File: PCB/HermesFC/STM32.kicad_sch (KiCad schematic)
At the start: 46 parts, among them J1 Conn_01x04, J2 Conn_01x04, J3 Conn_01x04, J4 Conn_01x04, J5 Conn_01x06, J6 USB_B_Micro, SW1 SW_Push, SW2 SW_SPDT, U1 STM32F405RGTx, U2 AMS1117-3.3, U3 USBLC6-2SC6, Y1 16Mhz

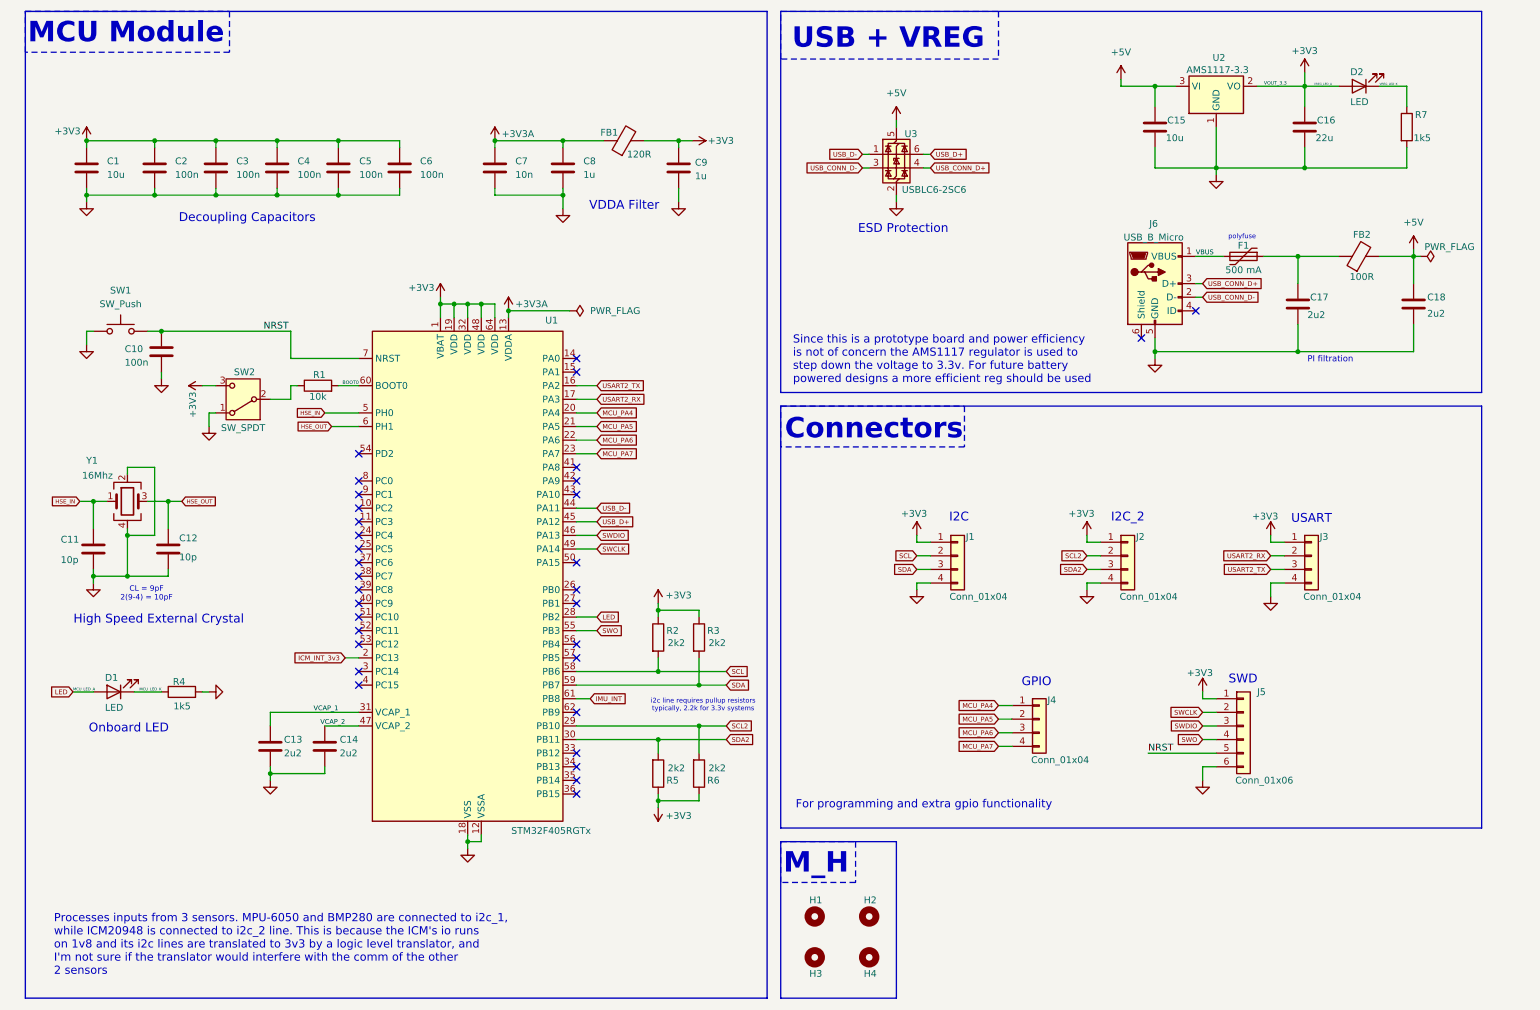
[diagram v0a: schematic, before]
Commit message: v0.2 updated schematic + PCB
added battery power source to PCB
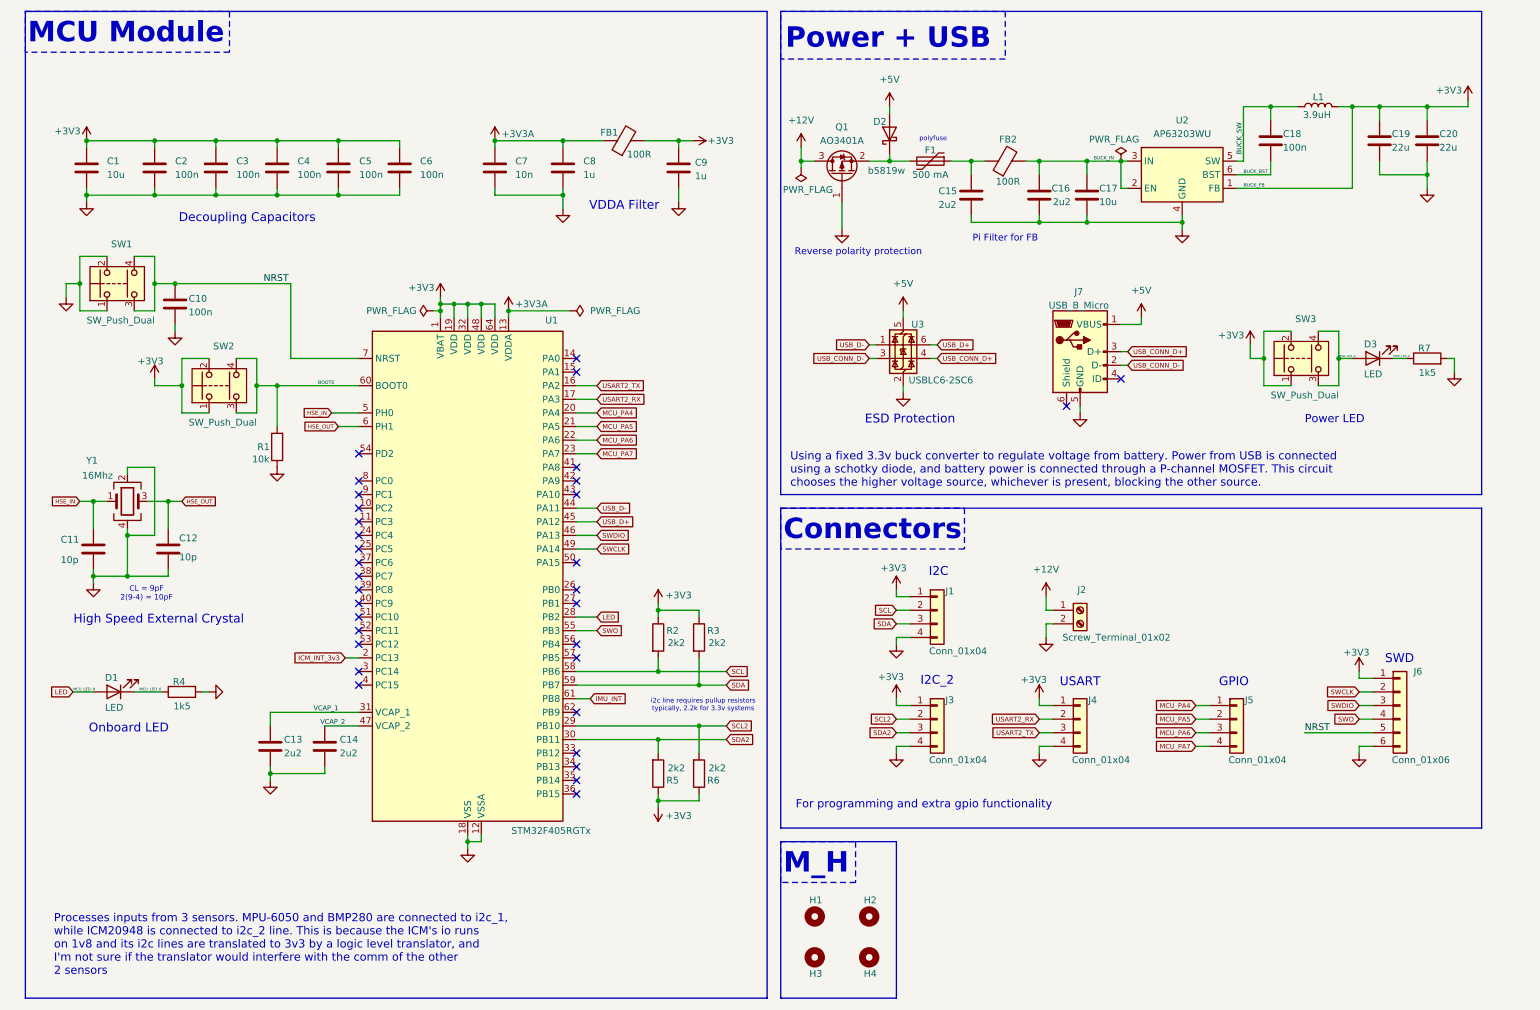
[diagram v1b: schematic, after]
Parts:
- removed C15: 10u, symbol Device:C
- removed C16: 22u, symbol Device:C
- removed D2: LED, symbol Device:LED
- removed SW1: SW_Push, symbol Switch:SW_Push
- removed SW2: SW_SPDT, symbol Switch:SW_SPDT
- removed U2: AMS1117-3.3, Package_TO_SOT_SMD:SOT-223-3_TabPin2, symbol Regulator_Linear:AMS1117-3.3
- added C17: 10u, Capacitor_SMD:C_0805_2012Metric, symbol Device:C
- added C18: 100n, Capacitor_SMD:C_0603_1608Metric_Pad1.08x0.95mm_HandSolder, symbol Device:C
- added C19, C20: 22u, Capacitor_SMD:C_0805_2012Metric, symbol Device:C
- added D2: b5819w, Diode_SMD:D_SOD-123, symbol Device:D_Schottky
- added D3: LED, LED_SMD:LED_0603_1608Metric, symbol Device:LED
- added J2: Screw_Terminal_01x02, TerminalBlock:TerminalBlock_Xinya_XY308-2.54-2P_1x02_P2.54mm_Horizontal, symbol Connector:Screw_Terminal_01x02
- added L1: 3.9uH, Inductor_SMD:L_Sunlord_SWPA4030S, symbol Device:L
- added Q1: AO3401A, Package_TO_SOT_SMD:SOT-23, symbol Transistor_FET:AO3401A
- added SW1, SW2, SW3: SW_Push_Dual, switch:KMR223GLFG, symbol Switch:SW_Push_Dual
- added U2: AP63203WU, Package_TO_SOT_SMD:TSOT-23-6, symbol Regulator_Switching:AP63203WU
- C1, C11, C12, C13, C14: footprint (none) -> Capacitor_SMD:C_0603_1608Metric
- C10, C2, C3, C4, C5, C6, C7, C8, C9: footprint (none) -> Capacitor_SMD:C_0402_1005Metric
- C15: renamed from C17; footprint (none) -> Capacitor_SMD:C_0603_1608Metric
- C16: renamed from C18; footprint (none) -> Capacitor_SMD:C_0603_1608Metric
- D1: footprint (none) -> LED_SMD:LED_0603_1608Metric
- F1: footprint (none) -> Fuse:Fuse_0603_1608Metric
- FB1: value 120R -> 100R; footprint (none) -> Inductor_SMD:L_0805_2012Metric
- FB2: footprint (none) -> Inductor_SMD:L_0805_2012Metric
- H1, H2, H3, H4: footprint (none) -> MountingHole:MountingHole_4.3mm_M4_Pad_Via
- J1: footprint (none) -> Connector_PinSocket_2.54mm:PinSocket_1x04_P2.54mm_Vertical
- J3: renamed from J2; footprint (none) -> Connector_PinSocket_2.54mm:PinSocket_1x04_P2.54mm_Vertical
- J4: renamed from J3; footprint (none) -> Connector_PinSocket_2.54mm:PinSocket_1x04_P2.54mm_Vertical
- J5: renamed from J4; footprint (none) -> Connector_PinSocket_2.54mm:PinSocket_1x04_P2.54mm_Vertical
- J6: renamed from J5; footprint (none) -> Connector_PinSocket_2.54mm:PinSocket_1x06_P2.54mm_Vertical
- J7: renamed from J6; footprint (none) -> Connector_USB:USB_Micro-B_Amphenol_10118193-0001LF_Horizontal
- R1: footprint (none) -> Resistor_SMD:R_0402_1005Metric
- R2, R3, R4, R5, R6, R7: footprint (none) -> Resistor_SMD:R_0603_1608Metric
- Y1: footprint (none) -> Crystal:Crystal_SMD_3225-4Pin_3.2x2.5mm
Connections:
- net +3V3: now also C19.1, C20.1, L1.2, SW2.1, SW2.2, SW3.1, SW3.2, U2.1 (FB)
- net +5V: now also J7.1 (VBUS), D2.2 (A); no longer C16.1, FB2.2
- net BOOT0: now also SW2.3, SW2.4
- net GND: now also R1.1, C17.2, C19.2, C20.2, J2.2 (Pin_2), Q1.1 (G), SW1.1, SW1.2, U2.4 (GND)
- net NRST: now also SW1.3, SW1.4
- net VBUS: no longer names the net of F1.2
- net VBUS: now also D2.1 (K), Q1.2 (S); no longer J7.1 (VBUS)
- net VREG_LED_K renamed POW_LED_K
- net POW_LED_K: now also D3.1 (K)
- new net +12V: J2.1 (Pin_1), Q1.3 (D)
- new net BUCK_BST: C18.2, U2.6 (BST)
- new net BUCK_IN: C16.1, C17.1, FB2.2, U2.2 (EN), U2.3 (IN)
- new net BUCK_SW: C18.1, L1.1, U2.5 (SW)
- new net POW_LED_A: D3.2 (A), SW3.3, SW3.4
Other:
- note added: "Pi Filter for FB"
- note added: "Power + USB"
- note added: "Power LED"
- note added: "Reverse polarity protection"
- note added: "Using a fixed 3.3v buck converter to regulate voltage from battery. Power from USB is connected using a schotky diode, and battery power is connected through a P-channel MOSFET. This circuit chooses the higher voltage source, whichever is present, blocking the other source."
- note removed: "PI filtration"
- note removed: "Since this is a prototype board and power efficiency is not of concern the AMS1117 regulator is used to step down the voltage to 3.3v. For future battery powered designs a more efficient reg should be used"
- note removed: "USB + VREG"
- moved on the sheet: C10, C15, C16, F1, FB2, J1, J3, J4, J5, J6, J7, R1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

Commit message: Updated design files for optimized BOM
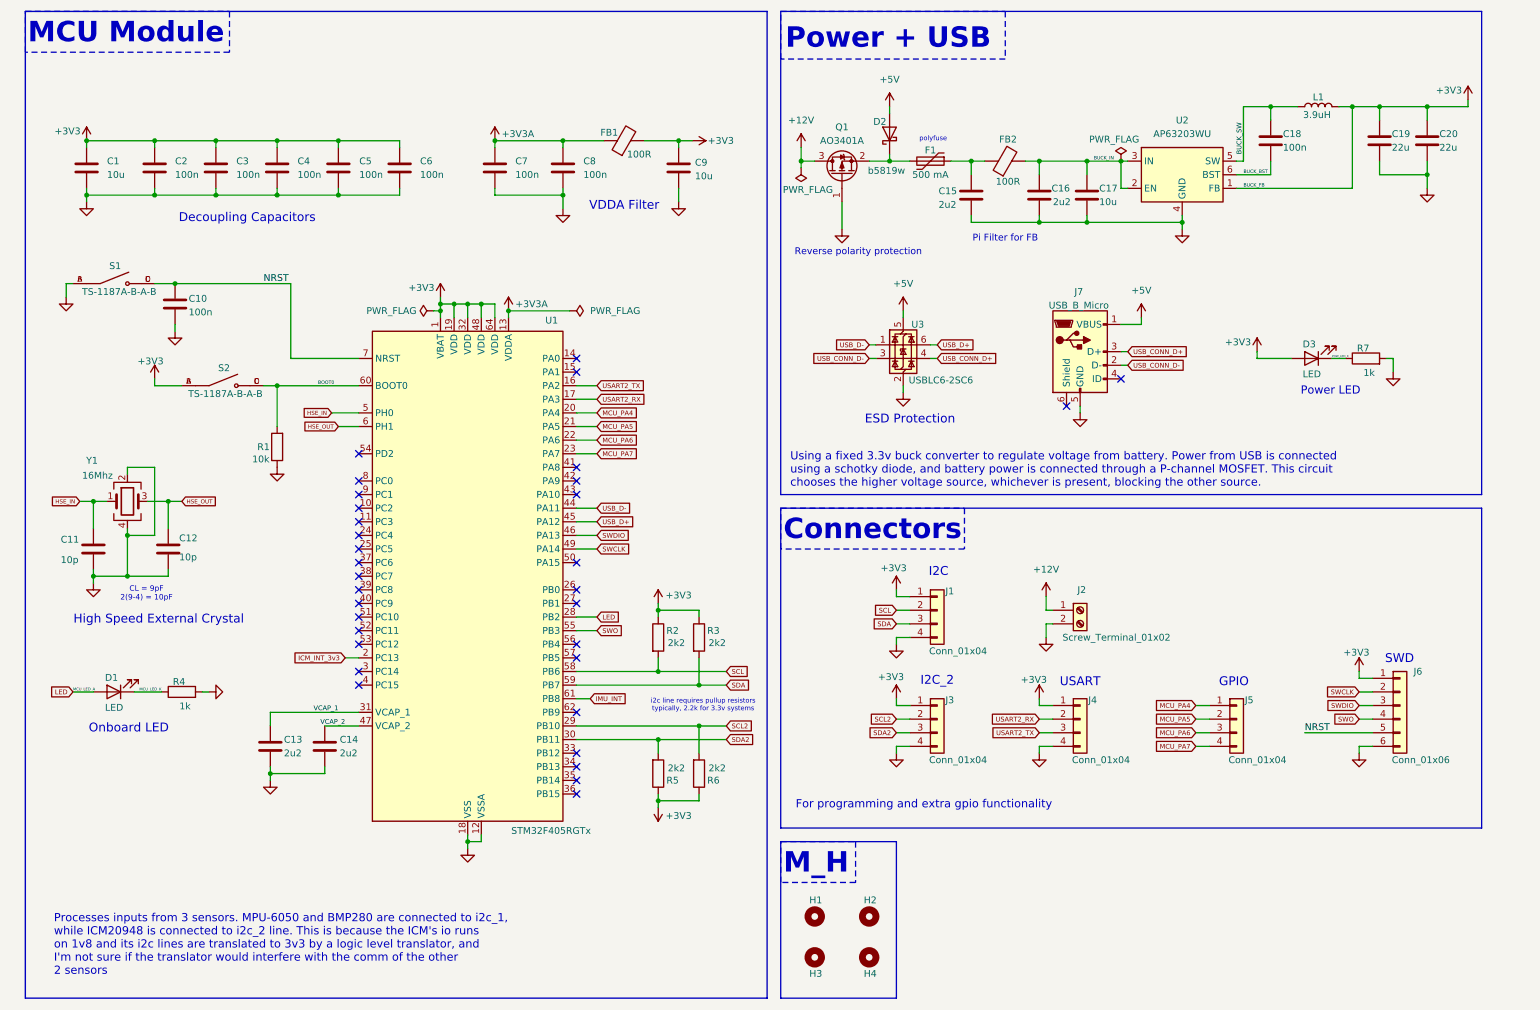
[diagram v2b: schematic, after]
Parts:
- removed SW1, SW2, SW3: SW_Push_Dual, switch:KMR223GLFG, symbol Switch:SW_Push_Dual
- added S1, S2: TS-1187A-B-A-B, switch:SW_TS-1187A-B-A-B, symbol TS-1187A-B-A-B:TS-1187A-B-A-B
- C17: footprint Capacitor_SMD:C_0805_2012Metric -> Capacitor_SMD:C_0603_1608Metric
- C18: footprint Capacitor_SMD:C_0603_1608Metric_Pad1.08x0.95mm_HandSolder -> Capacitor_SMD:C_0603_1608Metric
- C7: value 10n -> 100n
- C8: value 1u -> 100n
- C9: value 1u -> 10u; footprint Capacitor_SMD:C_0402_1005Metric -> Capacitor_SMD:C_0603_1608Metric
- R1: footprint Resistor_SMD:R_0402_1005Metric -> Resistor_SMD:R_0603_1608Metric
- R4, R7: value 1k5 -> 1k
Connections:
- net POW_LED_A is gone; now on net +3V3: D3.2 (A)
- net +3V3: now also S2.A, S2.B
- net BOOT0: now also S2.C, S2.D
- net GND: now also S1.A, S1.B
- net NRST: now also S1.C, S1.D
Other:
- moved on the sheet: D3, R7
